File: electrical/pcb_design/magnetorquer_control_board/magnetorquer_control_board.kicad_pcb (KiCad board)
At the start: 4 copper layers, 77 x 96 mm, 58 parts, among them J1 STLINK, J2 STLINK, J3 Molex_504050-1291, J4 External Power, J5 Molex_504050-1291, U1 STM32L452RCT6, U2 BMI323, U3 BMI323, U4 TCAN330DR, U5 INA260, U6 TLV76733DRVx

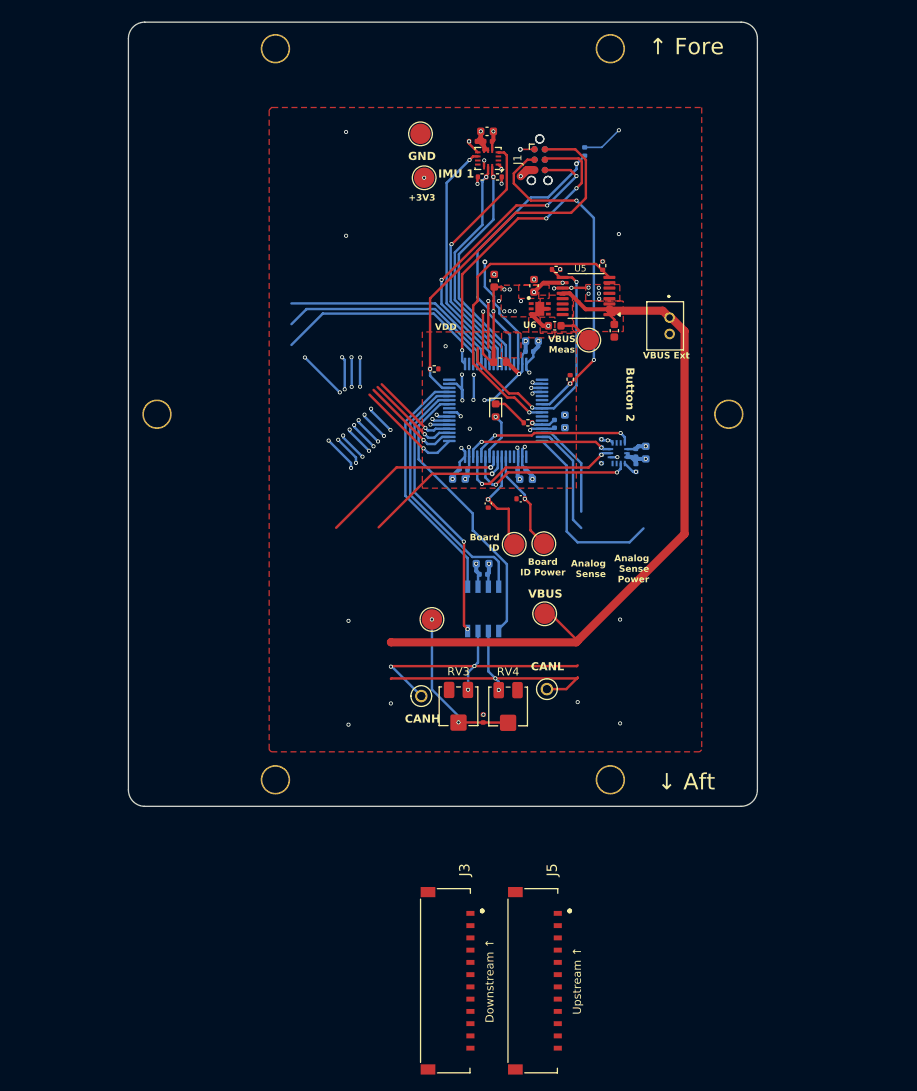
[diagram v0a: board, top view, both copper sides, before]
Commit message: Checkpoint progress on magnetorquer control board. All major facilities exist in the schematic. There may be some overlooked details, especially capacitors to reduce noise on power rails. Most of the components are laid out on the schematic, but unconnected.
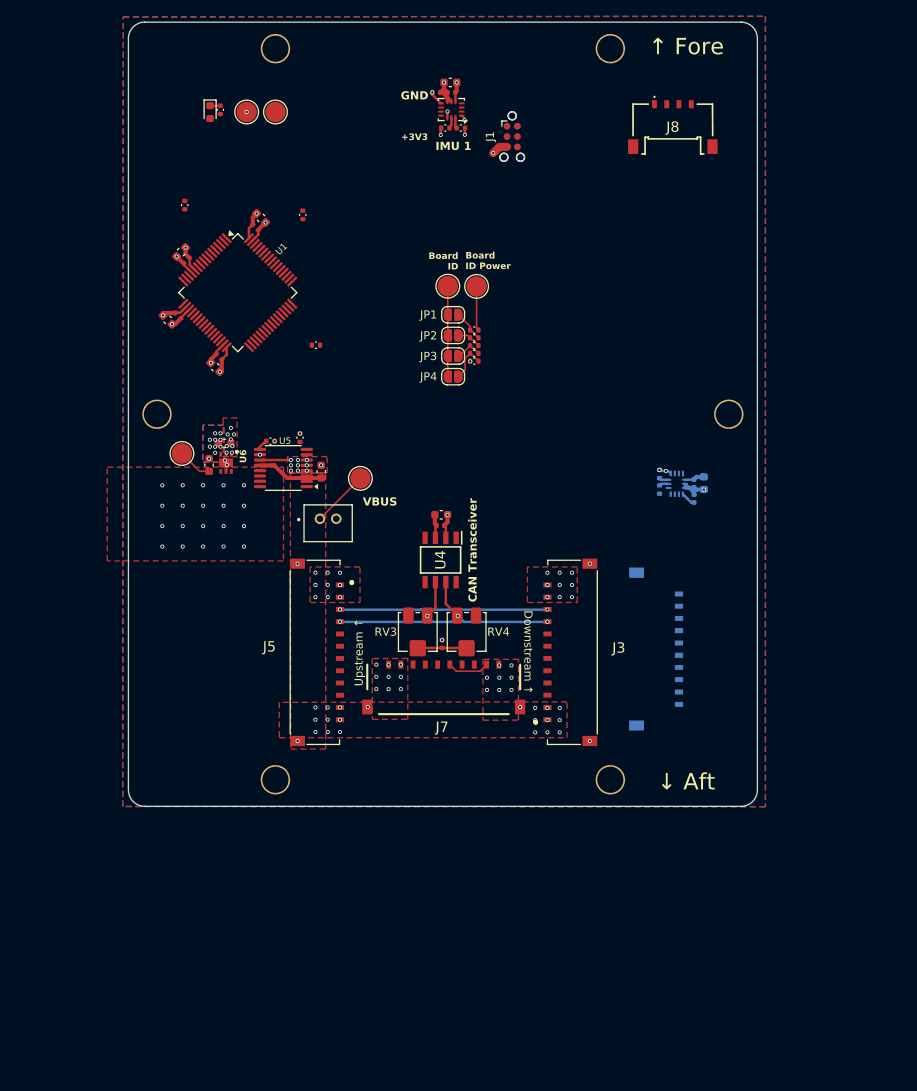
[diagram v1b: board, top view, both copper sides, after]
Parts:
- removed C18, C19: 10u, footprints:Nondescript_C_0603_1608Metric
- removed TP1, TP2: TestPoint, footprints:Keystone_5002
- removed TP12, TP9: TestPoint_Probe, footprints:TestPoint_Pad_D2.5mm
- added J6: Molex_504050-0891, footprints:Molex_504050-1091, B.Cu at (182.8, 133.7)
- added J7: Molex_504050-0891, footprints:Molex_504050-1091, F.Cu at (147.3, 128.8)
- added J8: Molex_504050-0491, footprints:Molex_504050-0491, F.Cu at (182.1, 63.2)
- added JP1: SolderJumper_2_Open, Jumper:SolderJumper-2_P1.3mm_Open_RoundedPad1.0x1.5mm, F.Cu at (155.2, 86.0)
- added JP2: SolderJumper_2_Open, Jumper:SolderJumper-2_P1.3mm_Open_RoundedPad1.0x1.5mm, F.Cu at (155.2, 88.5)
- added JP3: SolderJumper_2_Open, Jumper:SolderJumper-2_P1.3mm_Open_RoundedPad1.0x1.5mm, F.Cu at (155.2, 91.0)
- added JP4: SolderJumper_2_Open, Jumper:SolderJumper-2_P1.3mm_Open_RoundedPad1.0x1.5mm, F.Cu at (155.2, 93.5)
- added R13: R, footprints:Nondescript_R_0402_1005Metric, F.Cu at (157.8, 89.8)
- added R14: R, footprints:Nondescript_R_0402_1005Metric, F.Cu at (157.8, 90.7)
- added R15: R, footprints:Nondescript_R_0402_1005Metric, F.Cu at (157.8, 91.7)
- added TP7: TestPoint_Probe, footprints:TestPoint_Pad_D2.5mm, F.Cu at (158.1, 82.5)
- C10, C14, C15, C16, C17, C20, C21, C7, C8, C9, R10, U1, U4: moved to F.Cu
- moved R9 53.7 mm to (126.7, 60.9), turned to -90 degrees
- moved R8 51.8 mm to (122.3, 72.5)
- moved TP4 51.7 mm to (122.0, 103.0)
- moved C15 51.4 mm to (121.9, 78.3), turned to 45 degrees
- moved D1 50.5 mm to (125.4, 61.2)
- moved J4 49.4 mm to (138.9, 111.0), turned to 180 degrees
- moved C14 49.3 mm to (122.6, 79.3), turned to 45 degrees
- moved J5 48.2 mm to (138.3, 127.3)
- moved C17 48.0 mm to (120.2, 86.6), turned to 135 degrees
- moved C16 46.1 mm to (121.5, 86.1), turned to 135 degrees
- moved C2 45.6 mm to (125.3, 104.4), turned to 90 degrees
- moved J3 43.1 mm to (169.8, 127.3), turned to -90 degrees
- moved U6 42.8 mm to (127.4, 104.1), turned to -90 degrees
- moved R3 42.6 mm to (136.5, 101.0)
- moved U5 42.6 mm to (134.4, 104.7)
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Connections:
- net /BLUE_LED renamed /DEBUG_LED
- net Net-(U6-EN) renamed VCC
- net SPI3_CS1 renamed IMU2_SPI_CS
- net SPI3_CS2 renamed IMU1_SPI_CS
- R11 pad 1: /BOARD_ID_PWR -> BOARD_ID_PWR
- R11 pad 2: /BOARD_ID_SENS -> Net-(JP1-B)
- R12 pad 1: GND -> Net-(JP1-B)
- R12 pad 2: /BOARD_ID_SENS -> Net-(JP2-B)
- RV3 pad 3: CANH -> CANL
- RV4 pad 1: CANL -> CANH
- TP8 pad 1: /BOARD_ID_PWR -> BOARD_ID_SENS
- U1 pad 22: /BOARD_ID_PWR -> BOARD_ID_PWR
- U1 pad 23: /BOARD_ID_SENS -> BOARD_ID_SENS
- U1 pad 61: unconnected-(U1-PB8-Pad61) -> NMAG_FAULT
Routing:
- net GND: track 290.8 -> 36.4 mm, vias 57 -> 65
- net VBUS: track 90.2 -> 15.1 mm, vias 0 -> 18
- net +3V3: track 89.8 -> 27.4 mm, vias 44 -> 23
- net SWDIO: track 46.8 -> 0.00 mm, vias 1 -> 0
- net NRST: track 42.0 -> 0.00 mm, vias 3 -> 0
- net I2C3_SDA: track 39.2 -> 0.00 mm, vias 1 -> 0
- net TRACESWO: track 38.7 -> 0.00 mm, vias 3 -> 0
- net SWCLK: track 37.9 -> 0.00 mm, vias 3 -> 0
- net CAN1_SHUTDOWN: track 34.7 -> 0.00 mm
- net IMU1_INT1: track 34.3 -> 0.00 mm, vias 2 -> 0
- net BOOT0: track 33.8 -> 0.00 mm, vias 1 -> 0
- net CAN1_SILENT: track 33.2 -> 0.00 mm, vias 2 -> 0
- net CAN1_RX: track 32.2 -> 0.00 mm
- net I2C3_SCL: track 33.7 -> 1.51 mm, vias 2 -> 0
- net IMU1_INT2: track 31.9 -> 0.00 mm, vias 2 -> 0
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- added copper zone on In2.Cu, net +3V3
- added copper zone on B.Cu, net GND
- added copper zone on In1.Cu, net GND
- added copper zone on In2.Cu, net VBUS
- added copper zone on In2.Cu, net VCC
- removed copper zone on In1.Cu, net +3V3
- removed copper zone on In2.Cu, net GND
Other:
- board text removed: "Analog Sense"
- board text removed: "Analog Sense Power"
- board text removed: "Button 2"
- board text removed: "CANH"
- board text removed: "CANL"
- board text removed: "VBUS Ext"
- board text removed: "VBUS Meas"
- board text removed: "VDD"

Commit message: Checkpoint layout work on magnetorquer control board.
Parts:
- added JP10: SolderJumper_2_Open, Jumper:SolderJumper-2_P1.3mm_Open_RoundedPad1.0x1.5mm, F.Cu at (158.0, 64.8)
- added JP11: SolderJumper_2_Open, Jumper:SolderJumper-2_P1.3mm_Open_RoundedPad1.0x1.5mm, F.Cu at (150.3, 64.8)
- added JP12: SolderJumper_2_Open, Jumper:SolderJumper-2_P1.3mm_Open_RoundedPad1.0x1.5mm, F.Cu at (151.8, 60.9)
- added JP13: SolderJumper_2_Open, Jumper:SolderJumper-2_P1.3mm_Open_RoundedPad1.0x1.5mm, B.Cu at (177.7, 79.4)
- added JP14: SolderJumper_2_Open, Jumper:SolderJumper-2_P1.3mm_Open_RoundedPad1.0x1.5mm, B.Cu at (177.7, 86.1)
- added JP15: SolderJumper_2_Open, Jumper:SolderJumper-2_P1.3mm_Open_RoundedPad1.0x1.5mm, B.Cu at (177.7, 92.8)
- added JP16: SolderJumper_2_Open, Jumper:SolderJumper-2_P1.3mm_Open_RoundedPad1.0x1.5mm, B.Cu at (177.7, 99.5)
- added JP17: SolderJumper_2_Open, Jumper:SolderJumper-2_P1.3mm_Open_RoundedPad1.0x1.5mm, B.Cu at (177.7, 76.1)
- added JP18: SolderJumper_2_Open, Jumper:SolderJumper-2_P1.3mm_Open_RoundedPad1.0x1.5mm, B.Cu at (177.7, 82.8)
- added JP19: SolderJumper_2_Open, Jumper:SolderJumper-2_P1.3mm_Open_RoundedPad1.0x1.5mm, B.Cu at (177.7, 89.5)
- added JP20: SolderJumper_2_Open, Jumper:SolderJumper-2_P1.3mm_Open_RoundedPad1.0x1.5mm, B.Cu at (177.7, 96.2)
- added JP5: SolderJumper_2_Open, Jumper:SolderJumper-2_P1.3mm_Open_RoundedPad1.0x1.5mm, F.Cu at (159.0, 61.5)
- added JP6: SolderJumper_2_Open, Jumper:SolderJumper-2_P1.3mm_Open_RoundedPad1.0x1.5mm, F.Cu at (155.4, 64.8)
- added JP7: SolderJumper_2_Open, Jumper:SolderJumper-2_P1.3mm_Open_RoundedPad1.0x1.5mm, F.Cu at (152.9, 64.8)
- added JP8: SolderJumper_2_Open, Jumper:SolderJumper-2_P1.3mm_Open_RoundedPad1.0x1.5mm, F.Cu at (149.3, 60.9)
- added JP9: SolderJumper_2_Open, Jumper:SolderJumper-2_P1.3mm_Open_RoundedPad1.0x1.5mm, F.Cu at (159.0, 59.0)
- R10: moved to B.Cu
- moved R10 24.0 mm to (129.1, 96.5), turned to 45 degrees
- moved R2 23.3 mm to (175.9, 82.7), turned to 90 degrees
- moved R5 18.6 mm to (176.0, 89.3)
- moved C4 14.4 mm to (183.4, 92.3)
- moved C5 14.4 mm to (184.6, 92.3)
- moved C6 14.4 mm to (183.4, 94.1)
- moved U2 14.4 mm to (181.3, 92.3)
- moved J1 8.53 mm to (170.9, 63.2)
- moved J2 8.53 mm to (170.9, 63.2)
- moved TP8 8.05 mm to (148.6, 88.0)
- moved R4 5.95 mm to (148.6, 65.0), turned to -90 degrees
- moved R8 5.24 mm to (124.6, 77.3), turned to -135 degrees
- moved R7 4.24 mm to (136.2, 86.0), turned to -135 degrees
- moved R1 4.07 mm to (159.7, 65.0), turned to -90 degrees
- moved TP7 3.89 mm to (160.5, 85.5)
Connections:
- J8 pad 1: /Magnetorquer Control/VSOLAR_1_1 -> /Magnetorquer Control/VSOLAR_2_1
- J8 pad 2: /Magnetorquer Control/VSOLAR_1_2 -> /Magnetorquer Control/VSOLAR_2_2
- J8 pad 3: /Magnetorquer Control/VSOLAR_2_1 -> /Magnetorquer Control/VSOLAR_1_2
- J8 pad 4: /Magnetorquer Control/VSOLAR_2_2 -> /Magnetorquer Control/VSOLAR_1_1
- U2 pad 1: +3V3 -> Net-(JP13-A)
- U2 pad 12: +3V3 -> Net-(JP16-A)
- U2 pad 13: I2C2_SCL -> Net-(JP15-A)
- U2 pad 14: I2C2_SDA -> Net-(JP14-A)
- U3 pad 1: GND -> Net-(JP5-A)
- U3 pad 12: +3V3 -> Net-(JP12-A)
- U3 pad 13: I2C1_SCL -> Net-(JP11-A)
- U3 pad 14: I2C1_SDA -> Net-(JP10-A)
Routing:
- net I2C2_SDA: track 1.18 -> 169.8 mm, vias 0 -> 3
- net I2C2_SCL: track 1.18 -> 161.3 mm, vias 0 -> 3
- net NMAG_FAULT: track 5.16 -> 133.0 mm, vias 0 -> 3
- net I2C1_SDA: track 1.31 -> 97.0 mm, vias 0 -> 4
- net I2C1_SCL: track 1.15 -> 88.0 mm, vias 0 -> 4
- net /Magnetorquer Control/VSOLAR_2_2: track 0.00 -> 80.2 mm, vias 0 -> 2
- net /Magnetorquer Control/VSOLAR_2_1: track 0.00 -> 80.2 mm, vias 0 -> 2
- net IMU2_INT1: track 0.00 -> 75.6 mm, vias 0 -> 3
- net SPI3_SCK: track 0.00 -> 73.4 mm, vias 0 -> 2
- net /Magnetorquer Control/VSOLAR_1_1: track 0.00 -> 69.6 mm, vias 0 -> 2
- net SPI3_MOSI: track 0.00 -> 68.8 mm, vias 0 -> 2
- net /Magnetorquer Control/VSOLAR_1_2: track 0.00 -> 68.2 mm, vias 0 -> 2
- net SPI3_MISO: track 0.00 -> 67.8 mm, vias 0 -> 2
- net IMU2_INT2: track 0.00 -> 67.6 mm, vias 0 -> 3
- net BOOT0_CONTROL: track 0.00 -> 66.4 mm, vias 0 -> 2
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- added copper zone on B.Cu, net VCC
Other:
- board text removed: "+3V3"
- board text removed: "GND"

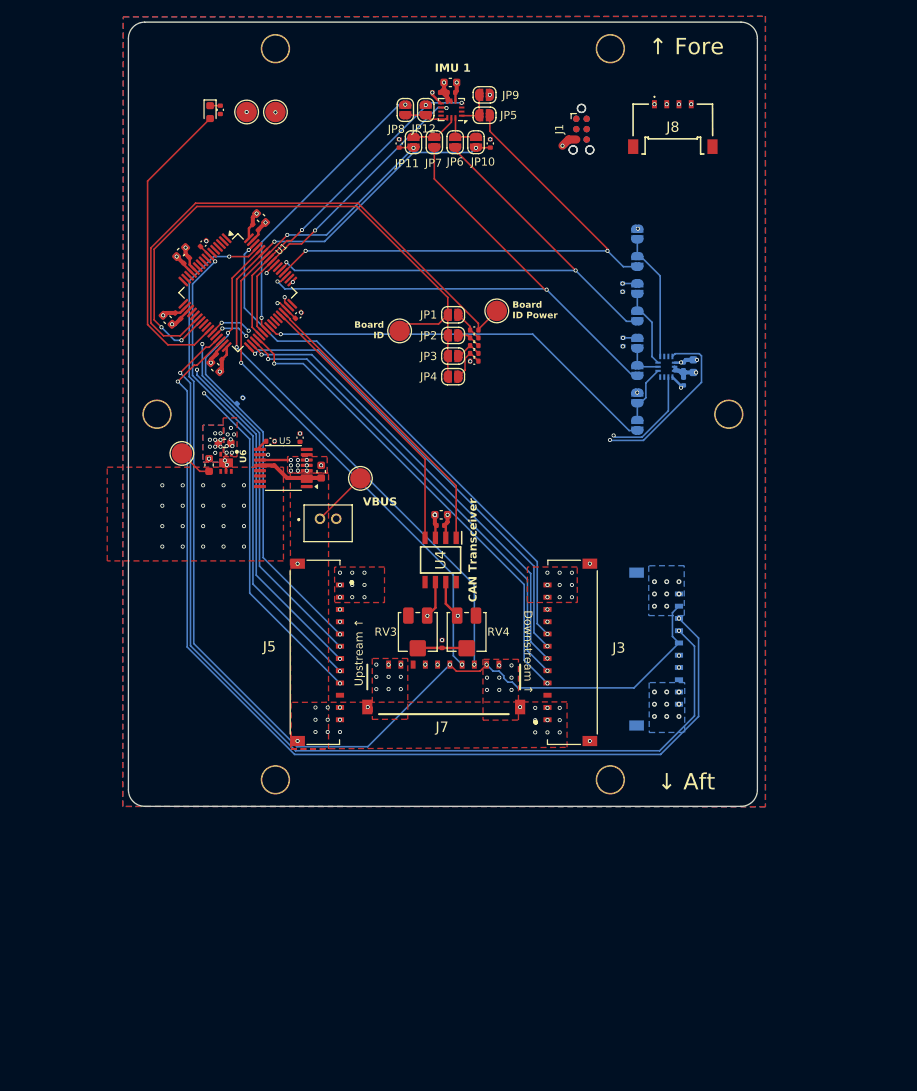
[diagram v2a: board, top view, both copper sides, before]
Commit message: Remove I2C bus from IMUs. We will use just SPI, rather than making the bus configurable. Remap the primary IMU interrupt lines to EXTIs with dedicated interrupts in the NVIC.
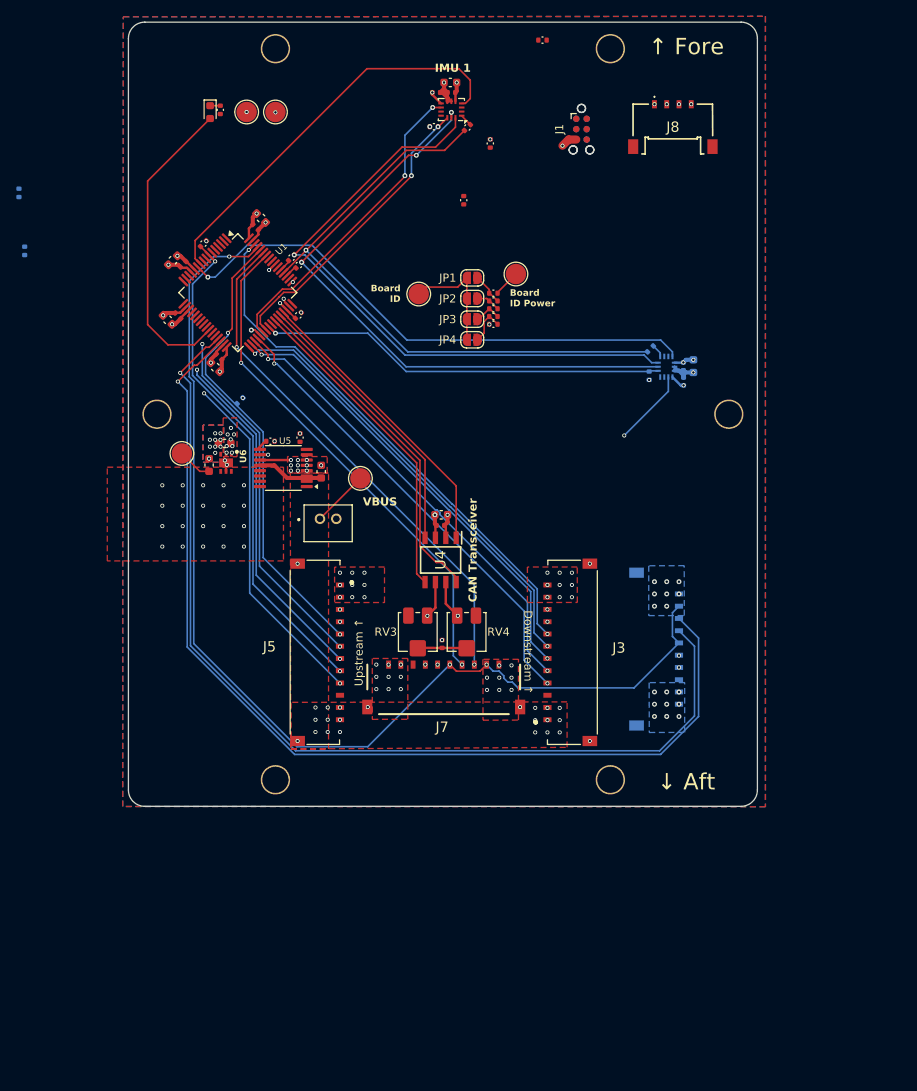
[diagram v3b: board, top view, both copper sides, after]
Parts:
- removed JP10, JP11, JP12, JP13, JP14, JP15, JP16, JP17, JP18, JP19, JP20, JP5, JP6, JP7, JP8, JP9: SolderJumper_2_Open, Jumper:SolderJumper-2_P1.3mm_Open_RoundedPad1.0x1.5mm
- added R16: 7.5k-10k, footprints:Nondescript_R_0402_1005Metric, F.Cu at (152.8, 63.0)
- added R17: 7.5k-10k, footprints:Nondescript_R_0402_1005Metric, B.Cu at (179.2, 93.4)
- added R18: 33, footprints:Nondescript_R_0402_1005Metric, F.Cu at (156.9, 63.0)
- added R19: 33, footprints:Nondescript_R_0402_1005Metric, F.Cu at (136.3, 79.9)
- added R20: 33, footprints:Nondescript_R_0402_1005Metric, F.Cu at (135.4, 79.0)
- added R21: 33, footprints:Nondescript_R_0402_1005Metric, B.Cu at (179.3, 90.2)
- added R22: 7.5k-10k, footprints:Nondescript_R_0402_1005Metric, F.Cu at (166.1, 52.4)
- R1, R2, R3, R4, R5, R6: value 7.5k -> 7.5k-10k
- R9: value 150 -> 33
- moved R2 74.8 mm to (102.0, 71.0)
- moved R5 74.1 mm to (102.7, 78.2)
- moved R4 10.5 mm to (156.5, 72.0)
- moved JP1 5.09 mm to (157.5, 81.5)
- moved JP2 5.09 mm to (157.5, 84.0)
- moved JP3 5.09 mm to (157.5, 86.5)
- moved JP4 5.09 mm to (157.5, 89.0)
- moved R11 5.09 mm to (160.1, 83.3)
- moved R12 5.09 mm to (160.1, 84.3)
- moved R13 5.09 mm to (160.1, 85.2)
- moved R14 5.09 mm to (160.1, 86.2)
- moved R15 5.09 mm to (160.1, 87.1)
- moved TP7 5.09 mm to (162.9, 81.0)
- moved TP8 5.09 mm to (151.0, 83.4)
- moved C15 1.42 mm to (120.9, 79.3)
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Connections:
- U1 pad 10: unconnected-(U1-PC2-Pad10) -> IMU1_INT1
- U1 pad 11: unconnected-(U1-PC3-Pad11) -> IMU2_INT1
- U1 pad 2: IMU2_INT1 -> unconnected-(U1-PC13-Pad2)
- U1 pad 27: IMU2_INT2 -> unconnected-(U1-PB1-Pad27)
- U1 pad 28: IMU2_INT1 -> unconnected-(U1-PB2-Pad28)
- U1 pad 3: IMU2_INT2 -> unconnected-(U1-PC14-Pad3)
- U1 pad 37: IMU1_INT1 -> IMU2_INT2
- U1 pad 51: SPI3_SCK -> Net-(U1-PC10)
- U1 pad 53: SPI3_MOSI -> Net-(U1-PC12)
- U1 pad 56: IMU1_INT2 -> unconnected-(U1-PB4-Pad56)
- U1 pad 57: IMU1_INT1 -> unconnected-(U1-PB5-Pad57)
- U2 pad 12: Net-(JP16-A) -> IMU2_SPI_CS
- U2 pad 13: Net-(JP15-A) -> SPI3_SCK
- U2 pad 14: Net-(JP14-A) -> SPI3_MOSI
- U3 pad 12: Net-(JP12-A) -> IMU1_SPI_CS
- U3 pad 13: Net-(JP11-A) -> SPI3_SCK
- U3 pad 14: Net-(JP10-A) -> SPI3_MOSI
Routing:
- net BOARD_ID_PWR: track 69.1 -> 3.18 mm
- net BOARD_ID_SENS: track 75.5 -> 14.3 mm, vias 2 -> 0
- net I2C2_SDA: track 169.8 -> 123.3 mm, vias 3 -> 1
- net CAN1_SILENT: track 0.00 -> 41.1 mm
- net I2C2_SCL: track 161.3 -> 120.3 mm, vias 3 -> 1
- net CAN1_SHUTDOWN: track 0.00 -> 39.6 mm
- net I2C1_SDA: track 97.0 -> 63.8 mm, vias 4 -> 2
- net I2C1_SCL: track 88.0 -> 62.6 mm, vias 4 -> 2
- net Net-(U2-SDO): track 15.7 -> 1.63 mm
- net Net-(JP14-A): track 9.68 -> 0.00 mm
- net IMU2_INT1: track 75.6 -> 66.2 mm, vias 3 -> 1
- net SPI3_MISO: track 67.8 -> 76.3 mm, vias 2 -> 1
- net SPI3_MOSI: track 68.8 -> 77.4 mm, vias 2 -> 1
- net IMU1_INT1: track 42.2 -> 49.7 mm, vias 2 -> 0
- net Net-(JP16-A): track 7.28 -> 0.00 mm
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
